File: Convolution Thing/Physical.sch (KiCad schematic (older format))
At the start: 8 parts

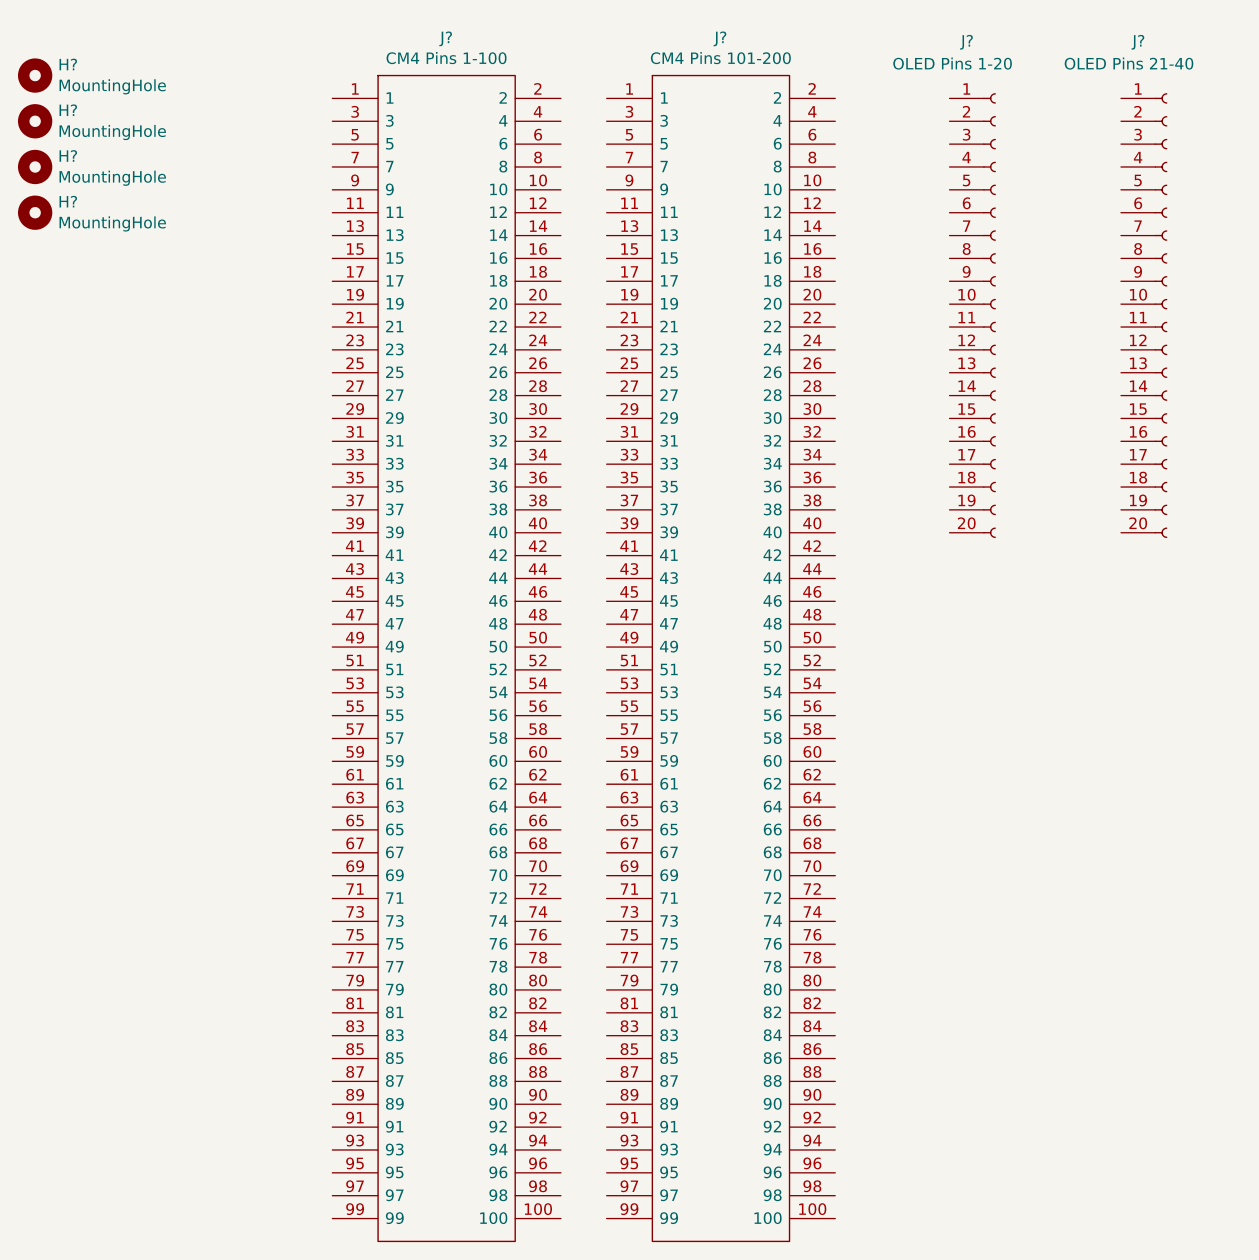
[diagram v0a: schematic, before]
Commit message: Fix some issues, add component references
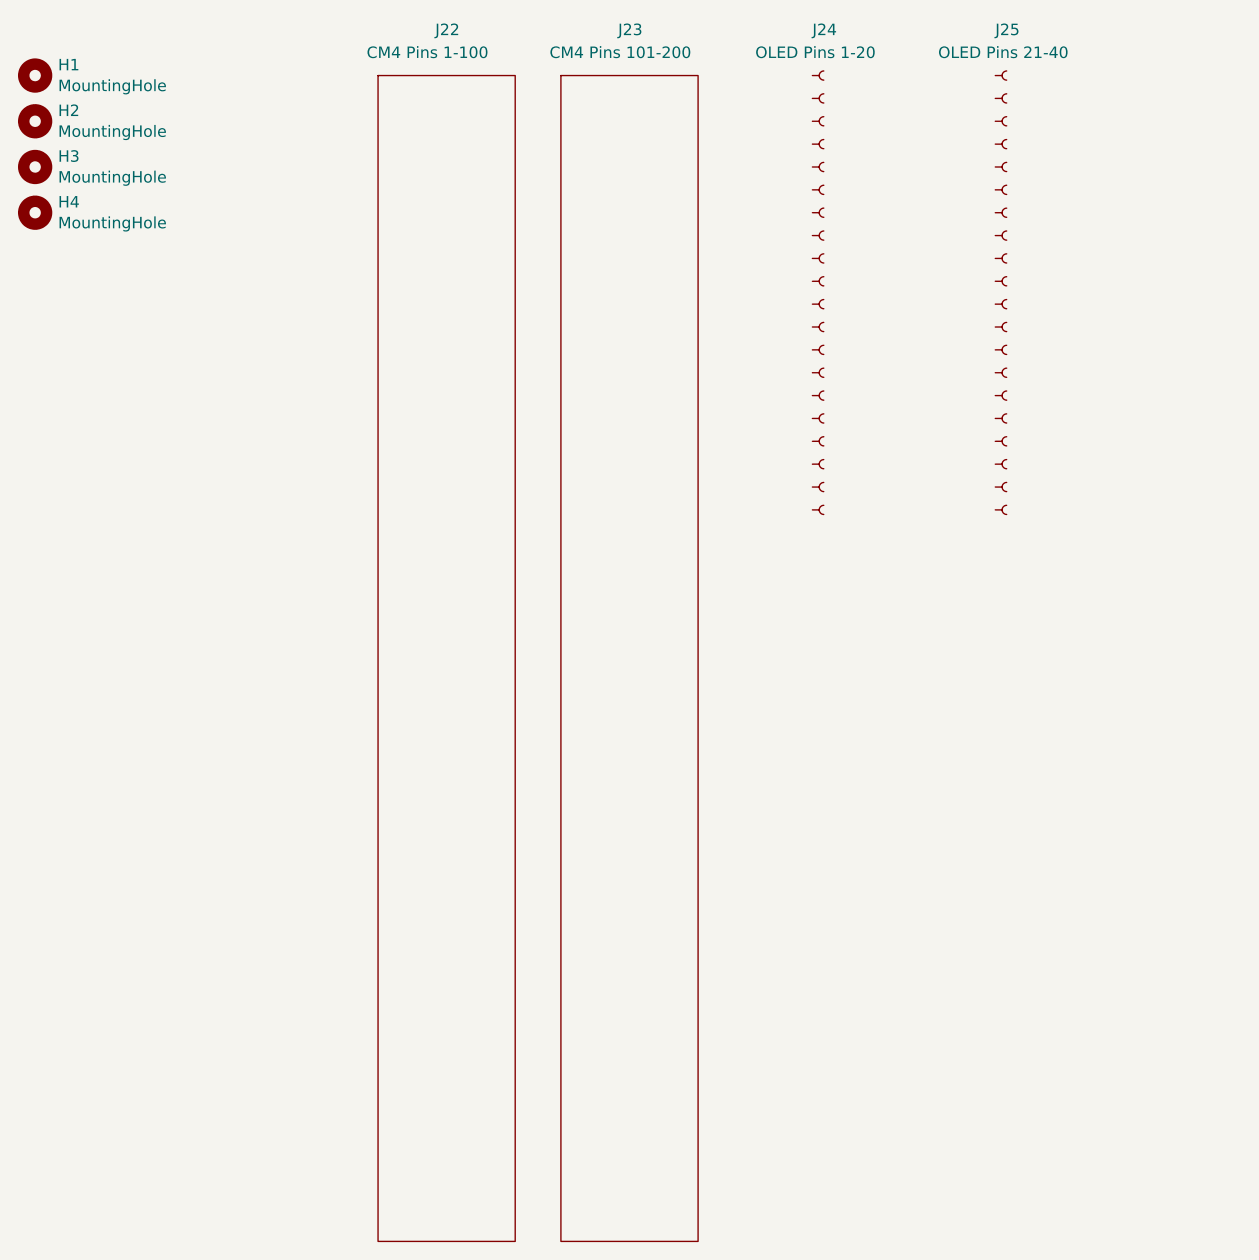
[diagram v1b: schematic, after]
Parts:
- removed J?: CM4 Pins 1-100, DF40C100DS04V58, symbol SamacSys:DF40C-100DS-0.4V_58_
- removed J?: CM4 Pins 101-200, DF40C100DS04V58, symbol SamacSys:DF40C-100DS-0.4V_58_
- removed J?: OLED Pins 1-20, symbol Connector:Conn_01x20_Female
- removed J?: OLED Pins 21-40, symbol Connector:Conn_01x20_Female
- added J22: CM4 Pins 1-100, DF40C100DS04V58, symbol Omat:DF40C-100DS-0.4V_Dummy
- added J23: CM4 Pins 101-200, DF40C100DS04V58, symbol Omat:DF40C-100DS-0.4V_Dummy
- added J24: OLED Pins 1-20, symbol Omat:Conn_01x20_Female_Dummy
- added J25: OLED Pins 21-40, symbol Omat:Conn_01x20_Female_Dummy
- gave numbers to parts that had none: 4
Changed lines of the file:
@@
 $EndDescr
 $Comp
-L Mechanical:MountingHole H?
+L Mechanical:MountingHole H1
 U 1 1 610EA3E1
 P 1000 1000
-F 0 "H?" H 1100 1046 50  0000 L CNN
+F 0 "H1" H 1100 1046 50  0000 L CNN
 F 1 "MountingHole" H 1100 955 50  0000 L CNN
 F 2 "" H 1000 1000 50  0001 C CNN
@@
 $EndComp
 $Comp
-L Mechanical:MountingHole H?
+L Mechanical:MountingHole H2
 U 1 1 610EA7CA
 P 1000 1200
-F 0 "H?" H 1100 1246 50  0000 L CNN
+F 0 "H2" H 1100 1246 50  0000 L CNN
 F 1 "MountingHole" H 1100 1155 50  0000 L CNN
 F 2 "" H 1000 1200 50  0001 C CNN
@@
 $EndComp
 $Comp
-L Mechanical:MountingHole H?
+L Mechanical:MountingHole H3
 U 1 1 610EA87F
 P 1000 1400
-F 0 "H?" H 1100 1446 50  0000 L CNN
+F 0 "H3" H 1100 1446 50  0000 L CNN
 F 1 "MountingHole" H 1100 1355 50  0000 L CNN
 F 2 "" H 1000 1400 50  0001 C CNN
@@
 $EndComp
 $Comp
-L Mechanical:MountingHole H?
+L Mechanical:MountingHole H4
 U 1 1 610EA934
 P 1000 1600
-F 0 "H?" H 1100 1646 50  0000 L CNN
+F 0 "H4" H 1100 1646 50  0000 L CNN
 F 1 "MountingHole" H 1100 1555 50  0000 L CNN
 F 2 "" H 1000 1600 50  0001 C CNN
@@
 $EndComp
 $Comp
-L SamacSys:DF40C-100DS-0.4V_58_ J?
-U 1 1 610EC383
+L Omat:DF40C-100DS-0.4V_Dummy J22
+U 1 1 6110CF8F
 P 2300 1100
-F 0 "J?" H 2800 1365 50  0000 C CNN
-F 1 "CM4 Pins 1-100" H 2800 1274 50  0000 C CNN
+F 0 "J22" H 2750 1400 50  0000 L CNN
+F 1 "CM4 Pins 1-100" H 2450 1300 50  0000 L CNN
 F 2 "DF40C100DS04V58" H 3150 1200 50  0001 L CNN
 F 3 "https://www.hirose.com/product/download/?distributor=digikey&type=specSheet&lang=en&num=DF40C-100DS-0.4V(58)" H 3150 1100 50  0001 L CNN
@@
 $EndComp
 $Comp
-L SamacSys:DF40C-100DS-0.4V_58_ J?
-U 1 1 610F161F
-P 3500 1100
-F 0 "J?" H 4000 1365 50  0000 C CNN
-F 1 "CM4 Pins 101-200" H 4000 1274 50  0000 C CNN
-F 2 "DF40C100DS04V58" H 4350 1200 50  0001 L CNN
-F 3 "https://www.hirose.com/product/download/?distributor=digikey&type=specSheet&lang=en&num=DF40C-100DS-0.4V(58)" H 4350 1100 50  0001 L CNN
-F 4 "Board to Board & Mezzanine Connectors 100POS 0.4MM SMD CONN RCPT GOLD" H 4350 1000 50  0001 L CNN "Description"
-F 5 "1.6" H 4350 900 50  0001 L CNN "Height"
-F 6 "798-DF40C100DS0.4V58" H 4350 800 50  0001 L CNN "Mouser Part Number"
-F 7 "https://www.mouser.co.uk/ProductDetail/Hirose-Connector/DF40C-100DS-04V58?qs=Gufeu08L%2Fl3EytQhkTt0gQ%3D%3D" H 4350 700 50  0001 L CNN "Mouser Price/Stock"
-F 8 "Hirose" H 4350 600 50  0001 L CNN "Manufacturer_Name"
-F 9 "DF40C-100DS-0.4V(58)" H 4350 500 50  0001 L CNN "Manufacturer_Part_Number"
-	1    3500 1100
+L Omat:DF40C-100DS-0.4V_Dummy J23
+U 1 1 6110D6EE
+P 3100 1100
+F 0 "J23" H 3550 1400 50  0000 L CNN
+F 1 "CM4 Pins 101-200" H 3250 1300 50  0000 L CNN
+F 2 "DF40C100DS04V58" H 3950 1200 50  0001 L CNN
+F 3 "https://www.hirose.com/product/download/?distributor=digikey&type=specSheet&lang=en&num=DF40C-100DS-0.4V(58)" H 3950 1100 50  0001 L CNN
+F 4 "Board to Board & Mezzanine Connectors 100POS 0.4MM SMD CONN RCPT GOLD" H 3950 1000 50  0001 L CNN "Description"
+F 5 "1.6" H 3950 900 50  0001 L CNN "Height"
+F 6 "798-DF40C100DS0.4V58" H 3950 800 50  0001 L CNN "Mouser Part Number"
+F 7 "https://www.mouser.co.uk/ProductDetail/Hirose-Connector/DF40C-100DS-04V58?qs=Gufeu08L%2Fl3EytQhkTt0gQ%3D%3D" H 3950 700 50  0001 L CNN "Mouser Price/Stock"
+F 8 "Hirose" H 3950 600 50  0001 L CNN "Manufacturer_Name"
+F 9 "DF40C-100DS-0.4V(58)" H 3950 500 50  0001 L CNN "Manufacturer_Part_Number"
+	1    3100 1100
 	1    0    0    -1
 $EndComp
 $Comp
-L Connector:Conn_01x20_Female J?
-U 1 1 610F84E3
-P 5200 2000
-F 0 "J?" H 5050 3150 50  0000 L CNN
-F 1 "OLED Pins 1-20" H 4750 3050 50  0000 L CNN
-F 2 "" H 5200 2000 50  0001 C CNN
-F 3 "~" H 5200 2000 50  0001 C CNN
-	1    5200 2000
+L Omat:Conn_01x20_Female_Dummy J24
+U 1 1 6111628A
+P 4450 1900
+F 0 "J24" H 4400 3000 50  0000 L CNN
+F 1 "OLED Pins 1-20" H 4150 2900 50  0000 L CNN
+F 2 "" H 4450 1900 50  0001 C CNN
+F 3 "~" H 4450 1900 50  0001 C CNN
+	1    4450 1900
 	1    0    0    -1
 $EndComp
 $Comp
-L Connector:Conn_01x20_Female J?
-U 1 1 610FA4A8
-P 5950 2000
-F 0 "J?" H 5800 3150 50  0000 L CNN
-F 1 "OLED Pins 21-40" H 5500 3050 50  0000 L CNN
-F 2 "" H 5950 2000 50  0001 C CNN
-F 3 "~" H 5950 2000 50  0001 C CNN
-	1    5950 2000
+L Omat:Conn_01x20_Female_Dummy J25
+U 1 1 6111AB29
+P 5250 1900
+F 0 "J25" H 5200 3000 50  0000 L CNN
+F 1 "OLED Pins 21-40" H 4950 2900 50  0000 L CNN
+F 2 "" H 5250 1900 50  0001 C CNN
+F 3 "~" H 5250 1900 50  0001 C CNN
+	1    5250 1900
 	1    0    0    -1
 $EndComp

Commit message: Started footprint assignment
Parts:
- J22, J23: footprint DF40C100DS04V58 -> SamacSys:DF40C100DS04V58
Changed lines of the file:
@@
 F 0 "J22" H 2750 1400 50  0000 L CNN
 F 1 "CM4 Pins 1-100" H 2450 1300 50  0000 L CNN
-F 2 "DF40C100DS04V58" H 3150 1200 50  0001 L CNN
+F 2 "SamacSys:DF40C100DS04V58" H 3150 1200 50  0001 L CNN
 F 3 "https://www.hirose.com/product/download/?distributor=digikey&type=specSheet&lang=en&num=DF40C-100DS-0.4V(58)" H 3150 1100 50  0001 L CNN
 F 4 "Board to Board & Mezzanine Connectors 100POS 0.4MM SMD CONN RCPT GOLD" H 3150 1000 50  0001 L CNN "Description"
@@
 F 0 "J23" H 3550 1400 50  0000 L CNN
 F 1 "CM4 Pins 101-200" H 3250 1300 50  0000 L CNN
-F 2 "DF40C100DS04V58" H 3950 1200 50  0001 L CNN
+F 2 "SamacSys:DF40C100DS04V58" H 3950 1200 50  0001 L CNN
 F 3 "https://www.hirose.com/product/download/?distributor=digikey&type=specSheet&lang=en&num=DF40C-100DS-0.4V(58)" H 3950 1100 50  0001 L CNN
 F 4 "Board to Board & Mezzanine Connectors 100POS 0.4MM SMD CONN RCPT GOLD" H 3950 1000 50  0001 L CNN "Description"

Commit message: Assign all footprints
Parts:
- H1, H2, H3, H4: footprint (none) -> MountingHole:MountingHole_4.3mm_M4
- J24, J25: footprint (none) -> Connector_PinHeader_2.54mm:PinHeader_1x20_P2.54mm_Vertical
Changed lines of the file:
@@
 F 0 "H1" H 1100 1046 50  0000 L CNN
 F 1 "MountingHole" H 1100 955 50  0000 L CNN
-F 2 "" H 1000 1000 50  0001 C CNN
+F 2 "MountingHole:MountingHole_4.3mm_M4" H 1000 1000 50  0001 C CNN
 F 3 "~" H 1000 1000 50  0001 C CNN
 	1    1000 1000
@@
 F 0 "H2" H 1100 1246 50  0000 L CNN
 F 1 "MountingHole" H 1100 1155 50  0000 L CNN
-F 2 "" H 1000 1200 50  0001 C CNN
+F 2 "MountingHole:MountingHole_4.3mm_M4" H 1000 1200 50  0001 C CNN
 F 3 "~" H 1000 1200 50  0001 C CNN
 	1    1000 1200
@@
 F 0 "H3" H 1100 1446 50  0000 L CNN
 F 1 "MountingHole" H 1100 1355 50  0000 L CNN
-F 2 "" H 1000 1400 50  0001 C CNN
+F 2 "MountingHole:MountingHole_4.3mm_M4" H 1000 1400 50  0001 C CNN
 F 3 "~" H 1000 1400 50  0001 C CNN
 	1    1000 1400
@@
 F 0 "H4" H 1100 1646 50  0000 L CNN
 F 1 "MountingHole" H 1100 1555 50  0000 L CNN
-F 2 "" H 1000 1600 50  0001 C CNN
+F 2 "MountingHole:MountingHole_4.3mm_M4" H 1000 1600 50  0001 C CNN
 F 3 "~" H 1000 1600 50  0001 C CNN
 	1    1000 1600
@@
 F 0 "J24" H 4400 3000 50  0000 L CNN
 F 1 "OLED Pins 1-20" H 4150 2900 50  0000 L CNN
-F 2 "" H 4450 1900 50  0001 C CNN
+F 2 "Connector_PinHeader_2.54mm:PinHeader_1x20_P2.54mm_Vertical" H 4450 1900 50  0001 C CNN
 F 3 "~" H 4450 1900 50  0001 C CNN
 	1    4450 1900
@@
 F 0 "J25" H 5200 3000 50  0000 L CNN
 F 1 "OLED Pins 21-40" H 4950 2900 50  0000 L CNN
-F 2 "" H 5250 1900 50  0001 C CNN
+F 2 "Connector_PinHeader_2.54mm:PinHeader_1x20_P2.54mm_Vertical" H 5250 1900 50  0001 C CNN
 F 3 "~" H 5250 1900 50  0001 C CNN
 	1    5250 1900

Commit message: PCB layout work and related changes to the schematic
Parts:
- renumbered J22 to J20, J23 to J21, J24 to J22, J25 to J23
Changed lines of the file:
@@
 $Descr A4 11693 8268
 encoding utf-8
-Sheet 13 13
+Sheet 12 13
 Title ""
 Date ""
@@
 $EndComp
 $Comp
-L Omat:DF40C-100DS-0.4V_Dummy J22
+L Omat:DF40C-100DS-0.4V_Dummy J20
 U 1 1 6110CF8F
 P 2300 1100
-F 0 "J22" H 2750 1400 50  0000 L CNN
+F 0 "J20" H 2750 1400 50  0000 L CNN
 F 1 "CM4 Pins 1-100" H 2450 1300 50  0000 L CNN
 F 2 "SamacSys:DF40C100DS04V58" H 3150 1200 50  0001 L CNN
@@
 $EndComp
 $Comp
-L Omat:DF40C-100DS-0.4V_Dummy J23
+L Omat:DF40C-100DS-0.4V_Dummy J21
 U 1 1 6110D6EE
 P 3100 1100
-F 0 "J23" H 3550 1400 50  0000 L CNN
+F 0 "J21" H 3550 1400 50  0000 L CNN
 F 1 "CM4 Pins 101-200" H 3250 1300 50  0000 L CNN
 F 2 "SamacSys:DF40C100DS04V58" H 3950 1200 50  0001 L CNN
@@
 $EndComp
 $Comp
-L Omat:Conn_01x20_Female_Dummy J24
+L Omat:Conn_01x20_Female_Dummy J22
 U 1 1 6111628A
 P 4450 1900
-F 0 "J24" H 4400 3000 50  0000 L CNN
+F 0 "J22" H 4400 3000 50  0000 L CNN
 F 1 "OLED Pins 1-20" H 4150 2900 50  0000 L CNN
 F 2 "Connector_PinHeader_2.54mm:PinHeader_1x20_P2.54mm_Vertical" H 4450 1900 50  0001 C CNN
@@
 $EndComp
 $Comp
-L Omat:Conn_01x20_Female_Dummy J25
+L Omat:Conn_01x20_Female_Dummy J23
 U 1 1 6111AB29
 P 5250 1900
-F 0 "J25" H 5200 3000 50  0000 L CNN
+F 0 "J23" H 5200 3000 50  0000 L CNN
 F 1 "OLED Pins 21-40" H 4950 2900 50  0000 L CNN
 F 2 "Connector_PinHeader_2.54mm:PinHeader_1x20_P2.54mm_Vertical" H 5250 1900 50  0001 C CNN

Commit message: PCB layout
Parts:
- removed J22: OLED Pins 1-20, Connector_PinHeader_2.54mm:PinHeader_1x20_P2.54mm_Vertical, symbol Omat:Conn_01x20_Female_Dummy
- removed J23: OLED Pins 21-40, Connector_PinHeader_2.54mm:PinHeader_1x20_P2.54mm_Vertical, symbol Omat:Conn_01x20_Female_Dummy
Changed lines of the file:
@@
-	1    0    0    -1
-$EndComp
-$Comp
-L Omat:Conn_01x20_Female_Dummy J22
-U 1 1 6111628A
-P 4450 1900
-F 0 "J22" H 4400 3000 50  0000 L CNN
-F 1 "OLED Pins 1-20" H 4150 2900 50  0000 L CNN
-F 2 "Connector_PinHeader_2.54mm:PinHeader_1x20_P2.54mm_Vertical" H 4450 1900 50  0001 C CNN
-F 3 "~" H 4450 1900 50  0001 C CNN
-	1    4450 1900
-	1    0    0    -1
-$EndComp
-$Comp
-L Omat:Conn_01x20_Female_Dummy J23
-U 1 1 6111AB29
-P 5250 1900
-F 0 "J23" H 5200 3000 50  0000 L CNN
-F 1 "OLED Pins 21-40" H 4950 2900 50  0000 L CNN
-F 2 "Connector_PinHeader_2.54mm:PinHeader_1x20_P2.54mm_Vertical" H 5250 1900 50  0001 C CNN
-F 3 "~" H 5250 1900 50  0001 C CNN
-	1    5250 1900
 	1    0    0    -1
 $EndComp
